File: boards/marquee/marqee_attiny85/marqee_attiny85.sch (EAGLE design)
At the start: 7 parts, among them U1 ATTINY85-20PU

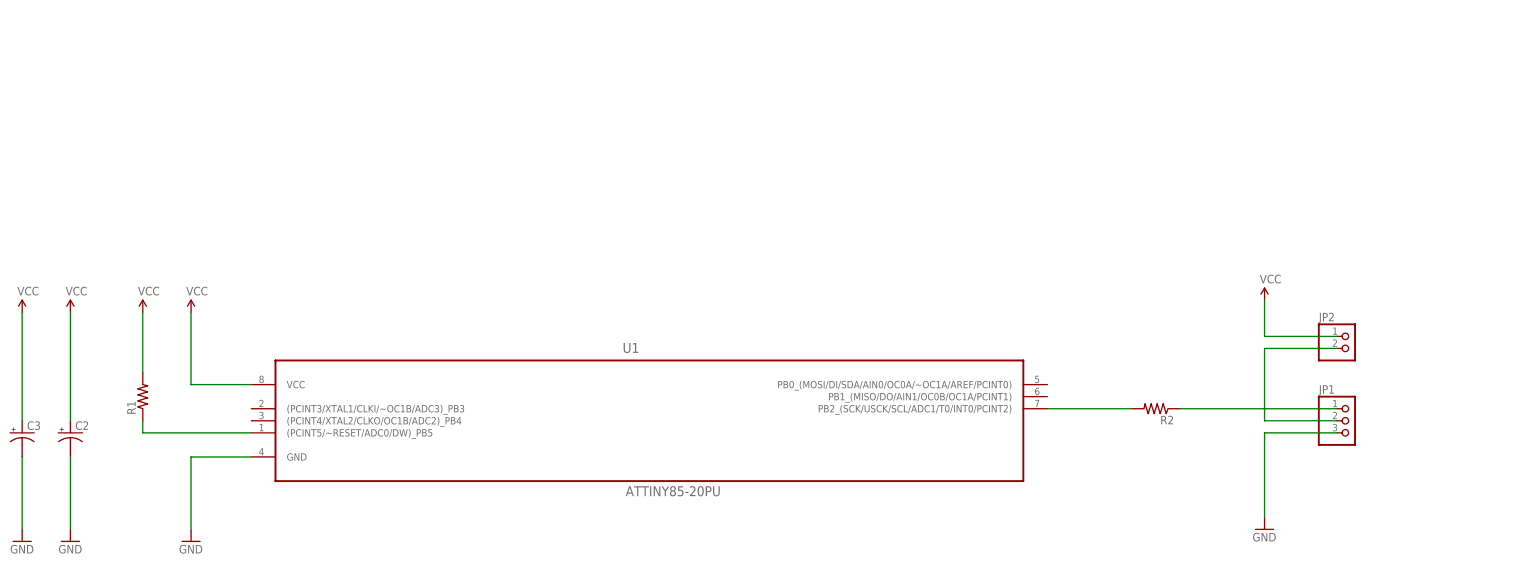
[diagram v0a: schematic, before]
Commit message: class 3 materials; adds Arrow-NeoPixel PCB
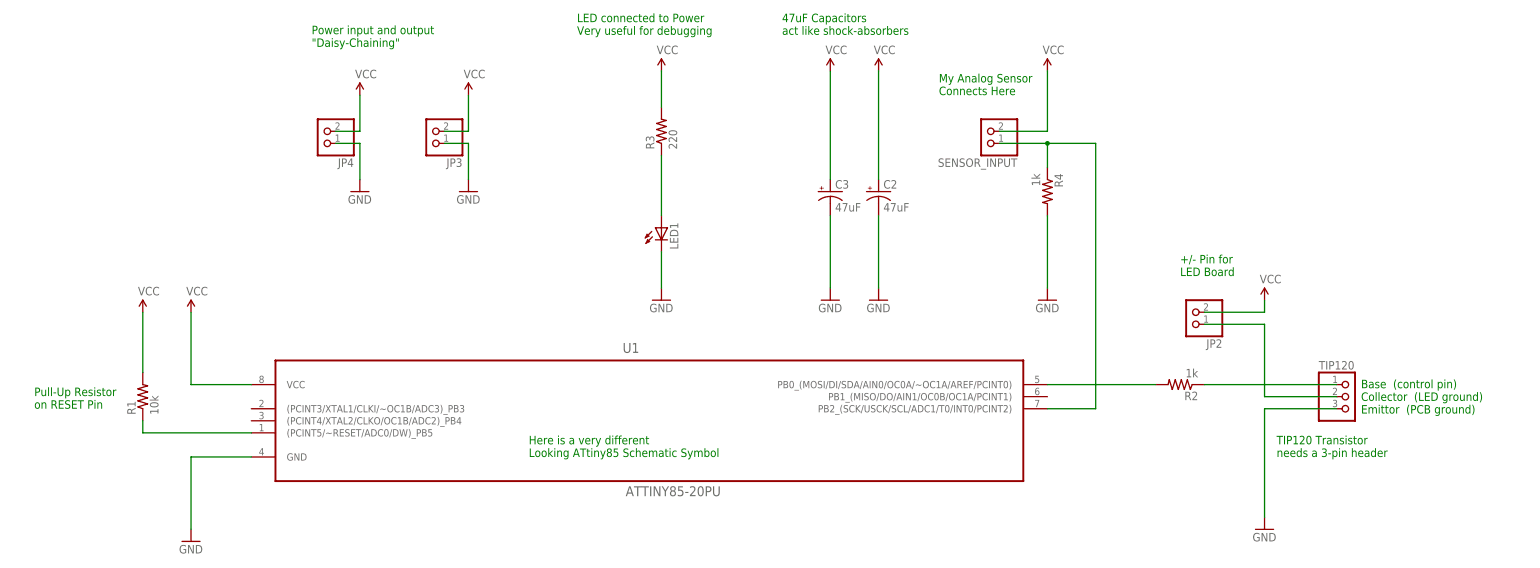
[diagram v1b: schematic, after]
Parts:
- removed JP1: (no value), pinhead:PINHD-1X3
- added JP3, JP4, SENSOR_INPUT: (no value), pinhead:PINHD-1X2
- added LED1: (no value), led:LED5MM
- added R3: 220, resistor:R-US_0207/10
- added R4: 1k, resistor:R-US_0207/10
- added TIP120: (no value), pinhead:PINHD-1X3
- C2, C3: value (none) -> 47uF
- R1: value (none) -> 10k
- R2: value (none) -> 1k
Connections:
- removed net N$6: JP1.2, JP2.2
- new net ANALOG_SENSOR_IN: R4.1, SENSOR_INPUT.1, U1.PB2_(SCK/USCK/SCL/ADC1/T0/INT0/PCINT2)
- new net N$3: LED1.A, R3.1
- new net THING: JP2.1, TIP120.2
- net GND: now also JP3.1, JP4.1, LED1.C, R4.2, TIP120.3; no longer JP1.3
- net N$2: now also TIP120.1; no longer JP1.1
- net N$4: now also U1.PB0_(MOSI/DI/SDA/AIN0/OC0A/~OC1A/AREF/PCINT0); no longer U1.PB2_(SCK/USCK/SCL/ADC1/T0/INT0/PCINT2)
- net VCC: now also JP2.2, JP3.2, JP4.2, R3.2, SENSOR_INPUT.2; no longer JP2.1
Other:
- note added: "+/- Pin for LED Board"
- note added: "47uF Capacitors act like shock-absorbers"
- note added: "Base (control pin) Collector (LED ground) Emittor (PCB ground)"
- note added: "Here is a very different Looking ATtiny85 Schematic Symbol"
- note added: "LED connected to Power Very useful for debugging"
- note added: "My Analog Sensor Connects Here"
- note added: "Power input and output "Daisy-Chaining""
- note added: "Pull-Up Resistor on RESET Pin"
- note added: "TIP120 Transistor needs a 3-pin header"
- moved on the sheet: C2, C3, JP2, R2
